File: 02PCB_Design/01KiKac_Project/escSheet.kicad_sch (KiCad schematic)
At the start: 1 part, among them J2 Screw_Terminal_01x03

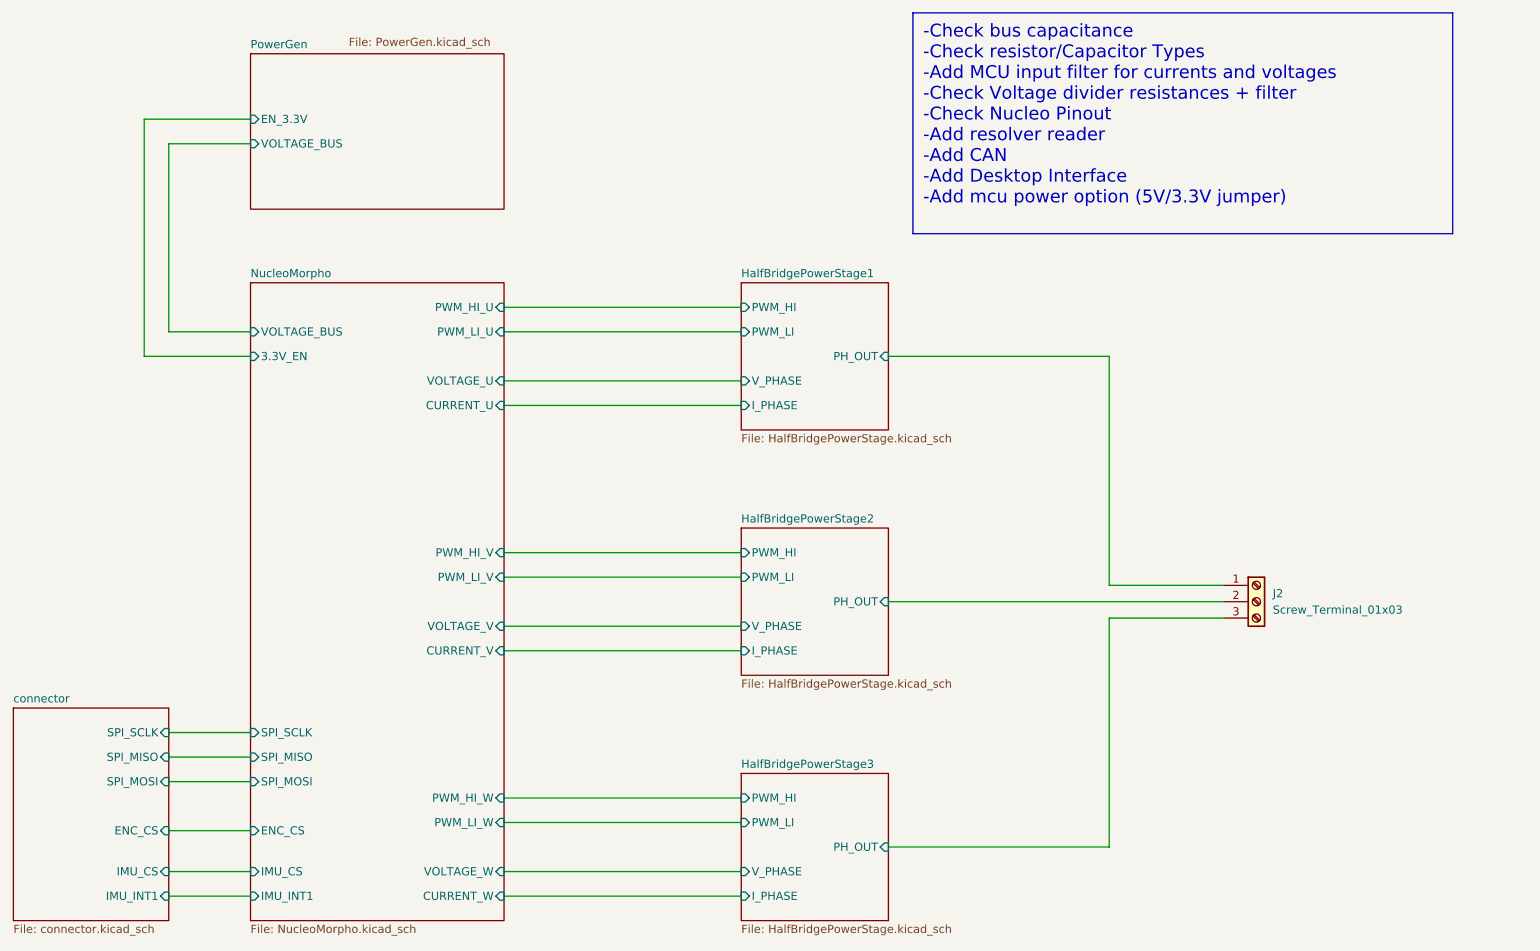
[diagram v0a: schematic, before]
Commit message: added CAN + minor changes
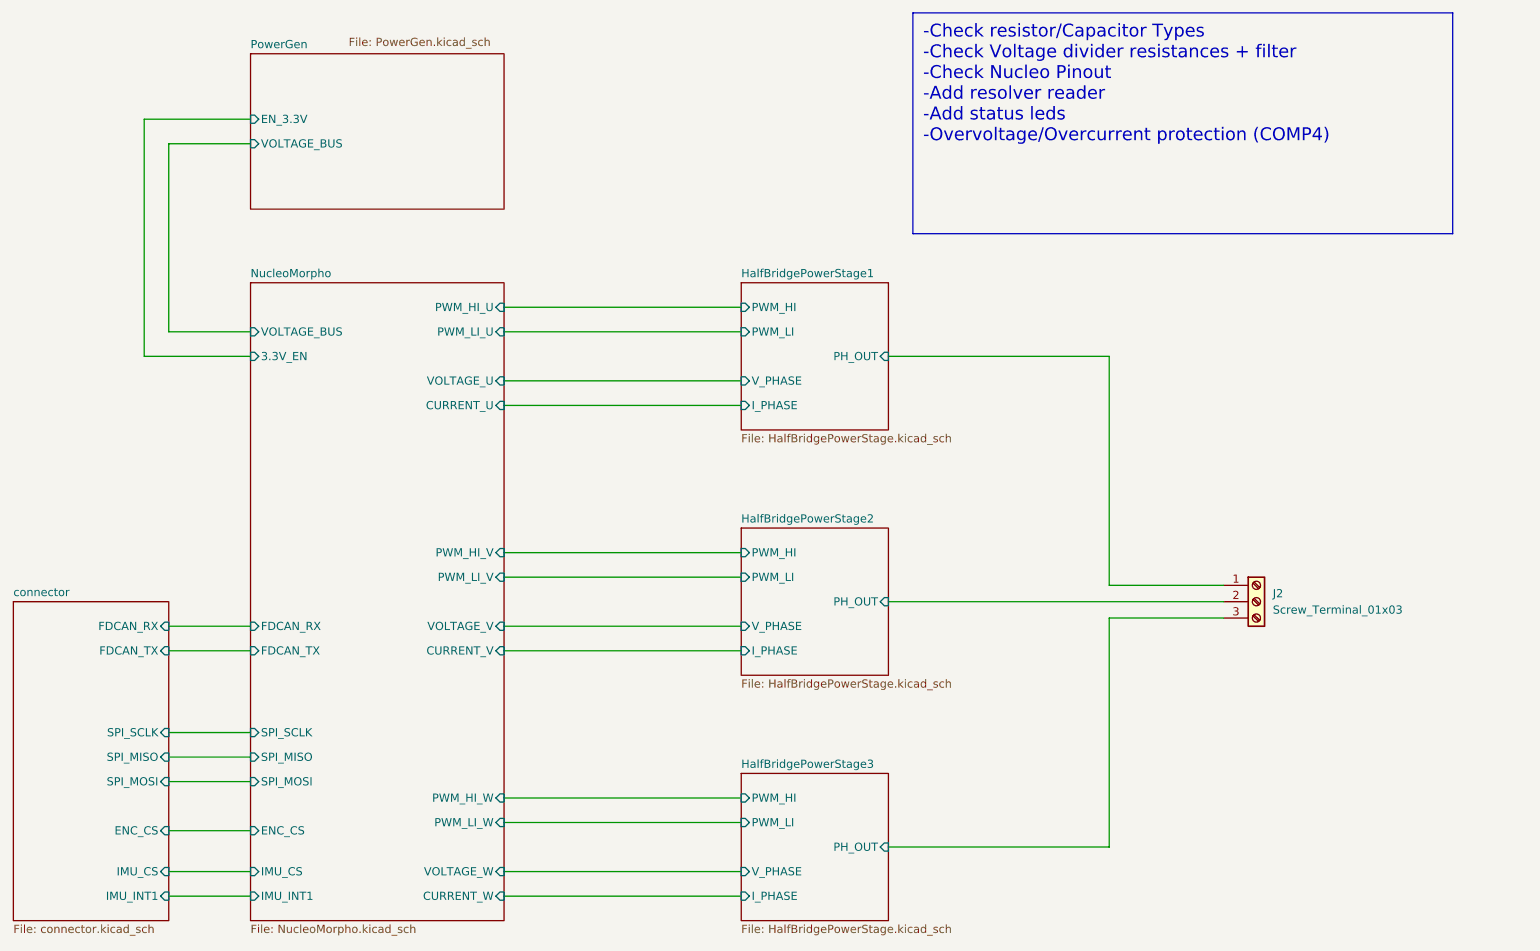
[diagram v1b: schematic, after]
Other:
- sheet NucleoMorpho ports: added FDCAN_RX, FDCAN_TX; removed none
- sheet connector ports: added FDCAN_RX, FDCAN_TX; removed none

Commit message: cleanup
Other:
- sheet connector renamed Bus_Connectors
- sheet Bus_Connectors ports: added O_ENC_A, O_ENC_B, O_ENC_I; removed none
- sheet NucleoMorpho ports: added O_ENC_A, O_ENC_B, O_ENC_I; removed none
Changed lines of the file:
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@@
     (stroke (width 0) (type default))
   )
-  (wire (pts (xy 82.55 64.77) (xy 82.55 35.56))
+  (wire (pts (xy 82.55 64.77) (xy 82.55 36.83))
     (stroke (width 0) (type default))
   )
@@
     (stroke (width 0) (type default))
   )
-  (wire (pts (xy 78.74 31.75) (xy 78.74 68.58))
+  (wire (pts (xy 78.74 33.02) (xy 78.74 68.58))
     (stroke (width 0) (type default))
   )
@@
     (stroke (width 0) (type default))
   )
-  (wire (pts (xy 82.55 35.56) (xy 95.25 35.56))
+  (wire (pts (xy 82.55 90.17) (xy 95.25 90.17))
+    (stroke (width 0) (type default))
+  )
+  (wire (pts (xy 82.55 93.98) (xy 95.25 93.98))
+    (stroke (width 0) (type default))
+  )
+  (wire (pts (xy 82.55 36.83) (xy 95.25 36.83))
     (stroke (width 0) (type default))
   )
@@
     (stroke (width 0) (type default))
   )
-  (wire (pts (xy 95.25 31.75) (xy 78.74 31.75))
+  (wire (pts (xy 95.25 33.02) (xy 78.74 33.02))
+    (stroke (width 0) (type default))
+  )
+  (wire (pts (xy 82.55 97.79) (xy 95.25 97.79))
     (stroke (width 0) (type default))
   )
@@
     (stroke (width 0) (type default))
   )
-  (text_box "-Check resistor/Capacitor Types\n-Check Voltage divider resistances + filter\n-Check Nucleo Pinout\n-Add resolver reader\n-Add status leds\n-Overvoltage/Overcurrent protection (COMP4)"
-    (at 198.12 15.24 0) (size 83.82 34.29)
+  (text_box "-Check resistor/Capacitor Types\n-Check Nucleo Pinout\n-Add resolver reader\n-Add status leds (Power lanes, Overcurrent fault)\n-Check reference designs"
+    (at 198.12 15.24 0) (size 83.82 21.59)
     (stroke (width 0) (type default))
     (fill (type none))
@@
     )
   )
+  (sheet (at 95.25 22.86) (size 39.37 24.13)
+    (stroke (width 0.1524) (type solid))
+    (fill (color 255 229 191 1.0000))
+    (property "Sheetname" "PowerGen" (at 95.25 22.1484 0)
+      (effects (font (size 1.27 1.27)) (justify left bottom))
+    )
+    (property "Sheetfile" "PowerGen.kicad_sch" (at 110.49 20.32 0)
+      (effects (font (size 1.27 1.27)) (justify left top))
+    )
+    (pin "EN_3.3V" input (at 95.25 33.02 180)
+      (effects (font (size 1.27 1.27)) (justify left))
+    )
+    (pin "VOLTAGE_BUS" input (at 95.25 36.83 180)
+      (effects (font (size 1.27 1.27)) (justify left))
+    )
+    (instances
+      (project "Testplatine"
+        (path "/de27a806-41f8-462d-8678-2476d523bbd9/a9fc49c7-f356-4c2b-bdd5-d12f8bcc20f7" (page "4"))
+      )
+    )
+  )
+  (sheet (at 58.42 86.36) (size 24.13 69.85) (fields_autoplaced)
+    (stroke (width 0.1524) (type solid))
+    (fill (color 255 229 191 1.0000))
+    (property "Sheetname" "Bus_Connectors" (at 58.42 85.6484 0)
+      (effects (font (size 1.27 1.27)) (justify left bottom))
+    )
+    (property "Sheetfile" "connector.kicad_sch" (at 58.42 156.7946 0)
+      (effects (font (size 1.27 1.27)) (justify left top))
+    )
+    (pin "ENC_CS" input (at 82.55 142.24 0)
+      (effects (font (size 1.27 1.27)) (justify right))
+    )
+    (pin "SPI_MOSI" input (at 82.55 134.62 0)
+      (effects (font (size 1.27 1.27)) (justify right))
+    )
+    (pin "SPI_SCLK" input (at 82.55 127 0)
+      (effects (font (size 1.27 1.27)) (justify right))
+    )
+    (pin "IMU_CS" input (at 82.55 148.59 0)
+      (effects (font (size 1.27 1.27)) (justify right))
+    )
+    (pin "SPI_MISO" input (at 82.55 130.81 0)
+      (effects (font (size 1.27 1.27)) (justify right))
+    )
+    (pin "IMU_INT1" input (at 82.55 152.4 0)
+      (effects (font (size 1.27 1.27)) (justify right))
+    )
+    (pin "FDCAN_RX" input (at 82.55 110.49 0)
+      (effects (font (size 1.27 1.27)) (justify right))
+    )
+    (pin "FDCAN_TX" input (at 82.55 114.3 0)
+      (effects (font (size 1.27 1.27)) (justify right))
+    )
+    (pin "O_ENC_I" input (at 82.55 97.79 0)
+      (effects (font (size 1.27 1.27)) (justify right))
+    )
+    (pin "O_ENC_B" input (at 82.55 93.98 0)
+      (effects (font (size 1.27 1.27)) (justify right))
+    )
+    (pin "O_ENC_A" input (at 82.55 90.17 0)
+      (effects (font (size 1.27 1.27)) (justify right))
+    )
+    (instances
+      (project "Testplatine"
+        (path "/de27a806-41f8-462d-8678-2476d523bbd9/a9fc49c7-f356-4c2b-bdd5-d12f8bcc20f7" (page "9"))
+      )
+    )
+  )
   (sheet (at 171.45 133.35) (size 22.86 22.86) (fields_autoplaced)
     (stroke (width 0.1524) (type solid))
@@
     )
   )
-  (sheet (at 95.25 21.59) (size 39.37 24.13)
-    (stroke (width 0.1524) (type solid))
-    (fill (color 255 229 191 1.0000))
-    (property "Sheetname" "PowerGen" (at 95.25 20.8784 0)
-      (effects (font (size 1.27 1.27)) (justify left bottom))
-    )
-    (property "Sheetfile" "PowerGen.kicad_sch" (at 110.49 19.05 0)
-      (effects (font (size 1.27 1.27)) (justify left top))
-    )
-    (pin "EN_3.3V" input (at 95.25 31.75 180)
-      (effects (font (size 1.27 1.27)) (justify left))
-    )
-    (pin "VOLTAGE_BUS" input (at 95.25 35.56 180)
-      (effects (font (size 1.27 1.27)) (justify left))
-    )
-    (instances
-      (project "Testplatine"
-        (path "/de27a806-41f8-462d-8678-2476d523bbd9/a9fc49c7-f356-4c2b-bdd5-d12f8bcc20f7" (page "4"))
-      )
-    )
-  )
-  (sheet (at 58.42 106.68) (size 24.13 49.53) (fields_autoplaced)
-    (stroke (width 0.1524) (type solid))
-    (fill (color 255 229 191 1.0000))
-    (property "Sheetname" "connector" (at 58.42 105.9684 0)
-      (effects (font (size 1.27 1.27)) (justify left bottom))
-    )
-    (property "Sheetfile" "connector.kicad_sch" (at 58.42 156.7946 0)
-      (effects (font (size 1.27 1.27)) (justify left top))
-    )
-    (pin "ENC_CS" input (at 82.55 142.24 0)
-      (effects (font (size 1.27 1.27)) (justify right))
-    )
-    (pin "SPI_MOSI" input (at 82.55 134.62 0)
-      (effects (font (size 1.27 1.27)) (justify right))
-    )
-    (pin "SPI_SCLK" input (at 82.55 127 0)
-      (effects (font (size 1.27 1.27)) (justify right))
-    )
-    (pin "IMU_CS" input (at 82.55 148.59 0)
-      (effects (font (size 1.27 1.27)) (justify right))
-    )
-    (pin "SPI_MISO" input (at 82.55 130.81 0)
-      (effects (font (size 1.27 1.27)) (justify right))
-    )
-    (pin "IMU_INT1" input (at 82.55 152.4 0)
-      (effects (font (size 1.27 1.27)) (justify right))
-    )
-    (pin "FDCAN_RX" input (at 82.55 110.49 0)
-      (effects (font (size 1.27 1.27)) (justify right))
-    )
-    (pin "FDCAN_TX" input (at 82.55 114.3 0)
-      (effects (font (size 1.27 1.27)) (justify right))
-    )
-    (instances
-      (project "Testplatine"
-        (path "/de27a806-41f8-462d-8678-2476d523bbd9/a9fc49c7-f356-4c2b-bdd5-d12f8bcc20f7" (page "9"))
+  (sheet (at 171.45 95.25) (size 22.86 22.86) (fields_autoplaced)
+    (stroke (width 0.1524) (type solid))
+    (fill (color 255 229 191 1.0000))
+    (property "Sheetname" "HalfBridgePowerStage2" (at 171.45 94.5384 0)
+      (effects (font (size 1.27 1.27)) (justify left bottom))
+    )
+    (property "Sheetfile" "HalfBridgePowerStage.kicad_sch" (at 171.45 118.6946 0)
+      (effects (font (size 1.27 1.27)) (justify left top))
+    )
+    (pin "PH_OUT" input (at 194.31 106.68 0)
+      (effects (font (size 1.27 1.27)) (justify right))
+    )
+    (pin "PWM_HI" input (at 171.45 99.06 180)
+      (effects (font (size 1.27 1.27)) (justify left))
+    )
+    (pin "PWM_LI" input (at 171.45 102.87 180)
+      (effects (font (size 1.27 1.27)) (justify left))
+    )
+    (pin "V_PHASE" input (at 171.45 110.49 180)
+      (effects (font (size 1.27 1.27)) (justify left))
+    )
+    (pin "I_PHASE" input (at 171.45 114.3 180)
+      (effects (font (size 1.27 1.27)) (justify left))
+    )
+    (instances
+      (project "Testplatine"
+        (path "/de27a806-41f8-462d-8678-2476d523bbd9/a9fc49c7-f356-4c2b-bdd5-d12f8bcc20f7" (page "6"))
       )
     )
@@
       (effects (font (size 1.27 1.27)) (justify left))
     )
+    (pin "O_ENC_A" input (at 95.25 90.17 180)
+      (effects (font (size 1.27 1.27)) (justify left))
+    )
+    (pin "O_ENC_B" input (at 95.25 93.98 180)
+      (effects (font (size 1.27 1.27)) (justify left))
+    )
+    (pin "O_ENC_I" input (at 95.25 97.79 180)
+      (effects (font (size 1.27 1.27)) (justify left))
+    )
     (instances
       (project "Testplatine"
@@
       )
     )
-  )
-  (sheet (at 171.45 95.25) (size 22.86 22.86) (fields_autoplaced)
-    (stroke (width 0.1524) (type solid))
-    (fill (color 255 229 191 1.0000))
-    (property "Sheetname" "HalfBridgePowerStage2" (at 171.45 94.5384 0)
-      (effects (font (size 1.27 1.27)) (justify left bottom))
-    )
-    (property "Sheetfile" "HalfBridgePowerStage.kicad_sch" (at 171.45 118.6946 0)
-      (effects (font (size 1.27 1.27)) (justify left top))
-    )
-    (pin "PH_OUT" input (at 194.31 106.68 0)
-      (effects (font (size 1.27 1.27)) (justify right))
-    )
-    (pin "PWM_HI" input (at 171.45 99.06 180)
-      (effects (font (size 1.27 1.27)) (justify left))
-    )
-    (pin "PWM_LI" input (at 171.45 102.87 180)
-      (effects (font (size 1.27 1.27)) (justify left))
-    )
-    (pin "V_PHASE" input (at 171.45 110.49 180)
-      (effects (font (size 1.27 1.27)) (justify left))
-    )
-    (pin "I_PHASE" input (at 171.45 114.3 180)
-      (effects (font (size 1.27 1.27)) (justify left))
-    )
-    (instances
-      (project "Testplatine"
-        (path "/de27a806-41f8-462d-8678-2476d523bbd9/a9fc49c7-f356-4c2b-bdd5-d12f8bcc20f7" (page "6"))
-      )
-    )
